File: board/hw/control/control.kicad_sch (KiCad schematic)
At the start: 41 parts, among them J1 stepper #1, J2 stepper #2, J3 buttons, J4 power, J6 AVR-ISP-10, Q1 MMFTP84W, Q2 MMFTP84W, U1 ULN2003A, U2 ULN2003A, U3 ULN2003A, U4 ULN2003A, U5 LM78L05_SO8

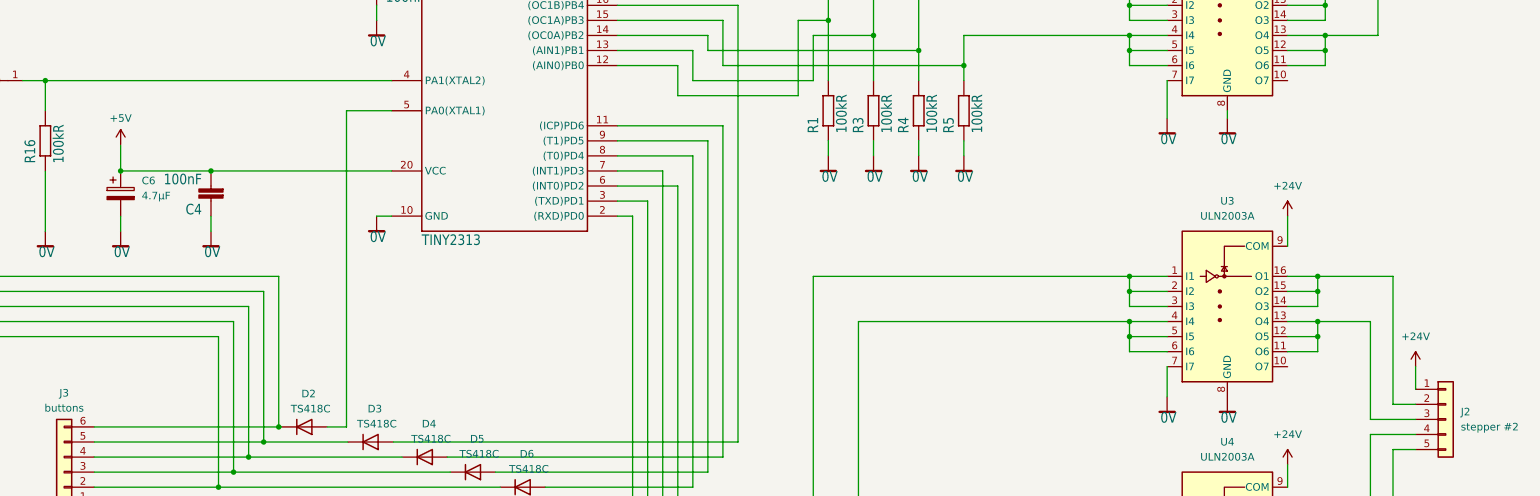
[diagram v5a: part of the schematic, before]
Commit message: added mount holes instead of vias + associated mess
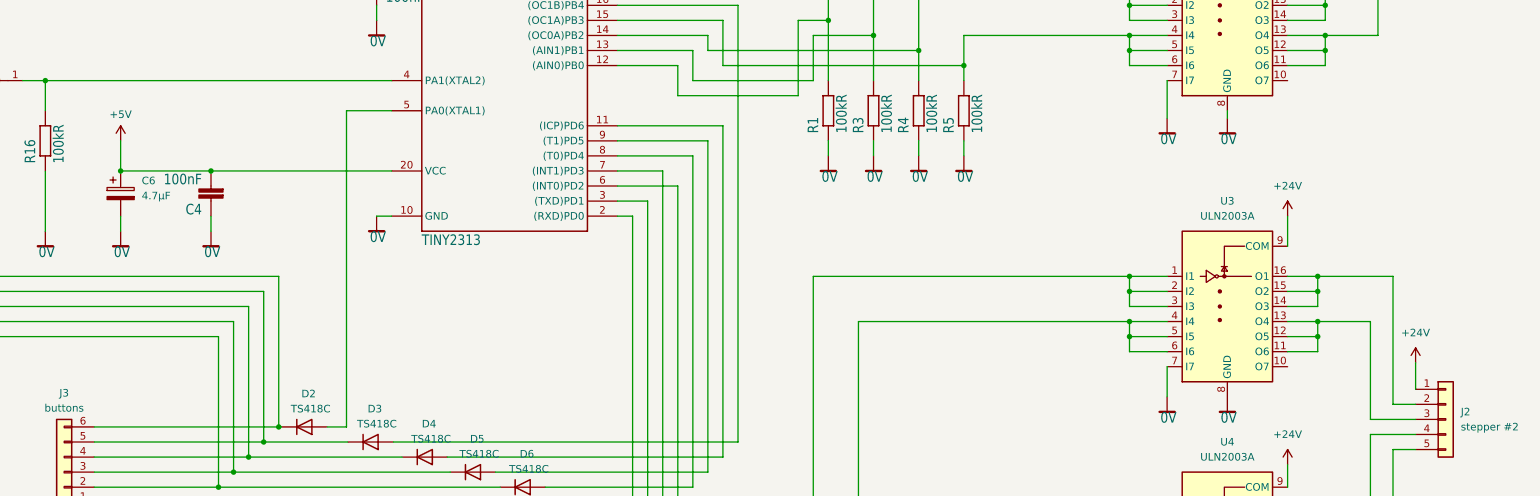
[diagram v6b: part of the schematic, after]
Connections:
- net +5V: now also C4.2, C6.1, U$1.20 (VCC)
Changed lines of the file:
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@@
   (junction (at 213.36 76.2) (diameter 0) (color 0 0 0 0)
   )
+  (junction (at 246.38 34.29) (diameter 0) (color 0 0 0 0)
+  )
+  (junction (at -22.86 64.77) (diameter 0) (color 0 0 0 0)
+  )
+  (junction (at 246.38 76.2) (diameter 0) (color 0 0 0 0)
+  )
+  (junction (at 213.36 29.21) (diameter 0) (color 0 0 0 0)
+  )
+  (junction (at 86.36 60.96) (diameter 0) (color 0 0 0 0)
+  )
+  (junction (at 213.36 68.58) (diameter 0) (color 0 0 0 0)
+  )
+  (junction (at 246.38 68.58) (diameter 0) (color 0 0 0 0)
+  )
+  (junction (at 245.11 160.02) (diameter 0) (color 0 0 0 0)
+  )
+  (junction (at 246.38 36.83) (diameter 0) (color 0 0 0 0)
+  )
   (junction (at 43.18 99.06) (diameter 0) (color 0 0 0 0)
   )
-  (junction (at 246.38 34.29) (diameter 0) (color 0 0 0 0)
-  )
-  (junction (at -22.86 64.77) (diameter 0) (color 0 0 0 0)
-  )
-  (junction (at 246.38 76.2) (diameter 0) (color 0 0 0 0)
-  )
-  (junction (at 213.36 29.21) (diameter 0) (color 0 0 0 0)
-  )
-  (junction (at 86.36 60.96) (diameter 0) (color 0 0 0 0)
-  )
-  (junction (at 213.36 68.58) (diameter 0) (color 0 0 0 0)
-  )
-  (junction (at 246.38 68.58) (diameter 0) (color 0 0 0 0)
-  )
-  (junction (at 245.11 160.02) (diameter 0) (color 0 0 0 0)
-  )
-  (junction (at 246.38 36.83) (diameter 0) (color 0 0 0 0)
-  )
   (junction (at 213.36 26.67) (diameter 0) (color 0 0 0 0)
   )
@@
     (stroke (width 0) (type default))
   )
-  (wire (pts (xy 261.62 132.08) (xy 261.62 135.89))
+  (wire (pts (xy 261.62 131.445) (xy 261.62 135.89))
     (stroke (width 0) (type default))
   )
@@
     (stroke (width 0) (type default))
   )
+  (wire (pts (xy 43.18 93.98) (xy 43.18 99.06))
+    (stroke (width 0) (type default))
+  )
   (wire (pts (xy -40.64 127) (xy 59.69 127))
     (stroke (width 0) (type default))
@@
   )
   (wire (pts (xy 252.095 52.705) (xy 252.095 68.58))
-    (stroke (width 0) (type default))
-  )
-  (wire (pts (xy 43.18 94.742) (xy 43.18 99.06))
     (stroke (width 0) (type default))
   )
@@
     )
   )
-  (symbol (lib_id "power:+24V") (at 261.62 132.08 0) (unit 1)
-    (in_bom yes) (on_board yes) (dnp no)
-    (property "Reference" "#PWR08" (at 261.62 135.89 0)
-      (effects (font (size 1.27 1.27)) hide)
-    )
-    (property "Value" "+24V" (at 261.62 127 0)
+  (symbol (lib_id "power:+24V") (at 261.62 131.445 0) (unit 1)
+    (in_bom yes) (on_board yes) (dnp no)
+    (property "Reference" "#PWR08" (at 261.62 135.255 0)
+      (effects (font (size 1.27 1.27)) hide)
+    )
+    (property "Value" "+24V" (at 261.62 126.365 0)
       (effects (font (size 1.27 1.27)))
     )
-    (property "Footprint" "" (at 261.62 132.08 0)
-      (effects (font (size 1.27 1.27)) hide)
-    )
-    (property "Datasheet" "" (at 261.62 132.08 0)
+    (property "Footprint" "" (at 261.62 131.445 0)
+      (effects (font (size 1.27 1.27)) hide)
+    )
+    (property "Datasheet" "" (at 261.62 131.445 0)
       (effects (font (size 1.27 1.27)) hide)
     )
@@
     )
   )
-  (symbol (lib_id "power:+5V") (at 43.18 94.615 0) (unit 1)
+  (symbol (lib_id "power:+5V") (at 43.18 93.98 0) (unit 1)
     (in_bom yes) (on_board yes) (dnp no) (fields_autoplaced)
-    (property "Reference" "#PWR01" (at 43.18 98.425 0)
-      (effects (font (size 1.27 1.27)) hide)
-    )
-    (property "Value" "+5V" (at 43.18 90.17 0)
+    (property "Reference" "#PWR01" (at 43.18 97.79 0)
+      (effects (font (size 1.27 1.27)) hide)
+    )
+    (property "Value" "+5V" (at 43.18 89.535 0)
       (effects (font (size 1.27 1.27)))
     )
-    (property "Footprint" "" (at 43.18 94.615 0)
-      (effects (font (size 1.27 1.27)) hide)
-    )
-    (property "Datasheet" "" (at 43.18 94.615 0)
-      (effects (font (size 1.27 1.27)) hide)
-    )
+    (property "Footprint" "" (at 43.18 93.98 0)
+      (effects (font (size 1.27 1.27)) hide)
+    )
+    (property "Datasheet" "" (at 43.18 93.98 0)
+      (effects (font (size 1.27 1.27)) hide)
+    )

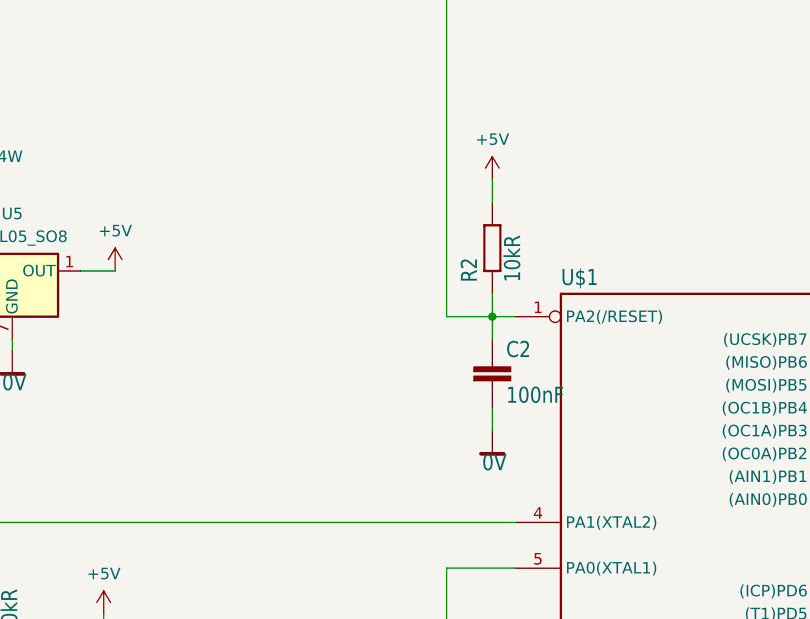
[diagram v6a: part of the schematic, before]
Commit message: added power-on LED to +5V line
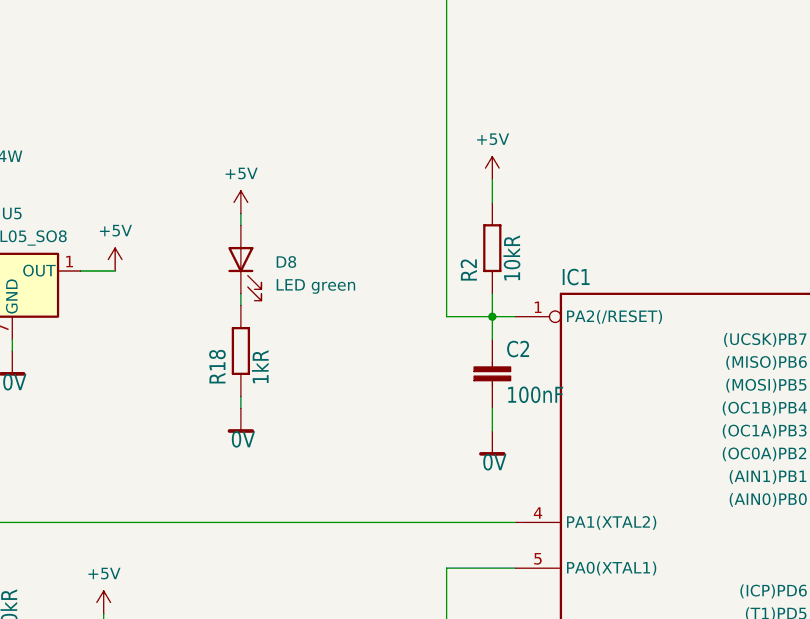
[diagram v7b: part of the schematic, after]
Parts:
- added D8: LED green, LED_SMD:LED_0805_2012Metric_Pad1.15x1.40mm_HandSolder, symbol Device:LED
- added R18: 1kR, Resistor_SMD:R_0805_2012Metric_Pad1.20x1.40mm_HandSolder, symbol control-eagle-import:R-EU_MELF0204W
- renumbered U$1 to IC1
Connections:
- net +5V: now also D8.2 (A)
- net 0V: now also R18.1
- new net: D8.1 (K), R18.2
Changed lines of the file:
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@@
+    (stroke (width 0) (type default))
+  )
+  (wire (pts (xy 58.42 58.42) (xy 58.42 59.69))
     (stroke (width 0) (type default))
   )
@@
     (stroke (width 0) (type default))
   )
+  (wire (pts (xy 58.42 49.53) (xy 58.42 50.8))
+    (stroke (width 0) (type default))
+  )
   (wire (pts (xy 10.795 34.29) (xy 20.32 34.29))
     (stroke (width 0) (type default))
@@
     (stroke (width 0) (type default))
   )
+  (wire (pts (xy 58.42 69.85) (xy 58.42 71.12))
+    (stroke (width 0) (type default))
+  )
   (symbol (lib_id "control-eagle-import:0V") (at 17.78 67.31 0) (unit 1)
     (in_bom yes) (on_board yes) (dnp no)
@@
         (path "/99b3aba4-a2cc-4425-a477-43f3a410d922"
           (reference "R10") (unit 1)
+        )
+      )
+    )
+  )
+  (symbol (lib_id "Device:LED") (at 58.42 54.61 90) (unit 1)
+    (in_bom yes) (on_board yes) (dnp no) (fields_autoplaced)
+    (property "Reference" "D8" (at 62.23 54.9275 90)
+      (effects (font (size 1.27 1.27)) (justify right))
+    )
+    (property "Value" "LED green" (at 62.23 57.4675 90)
+      (effects (font (size 1.27 1.27)) (justify right))
+    )
+    (property "Footprint" "LED_SMD:LED_0805_2012Metric_Pad1.15x1.40mm_HandSolder" (at 58.42 54.61 0)
+      (effects (font (size 1.27 1.27)) hide)
+    )
+    (property "Datasheet" "~" (at 58.42 54.61 0)
+      (effects (font (size 1.27 1.27)) hide)
+    )
+    (pin "1")
+    (pin "2")
+    (instances
+      (project "control"
+        (path "/99b3aba4-a2cc-4425-a477-43f3a410d922"
+          (reference "D8") (unit 1)
         )
       )
@@
     )
   )
+  (symbol (lib_id "control-eagle-import:0V") (at 58.42 73.66 0) (unit 1)
+    (in_bom yes) (on_board yes) (dnp no)
+    (property "Reference" "#SUPPLY021" (at 58.42 73.66 0)
+      (effects (font (size 1.27 1.27)) hide)
+    )
+    (property "Value" "0V" (at 57.277 75.692 0)
+      (effects (font (size 1.778 1.5113)) (justify left bottom))
+    )
+    (property "Footprint" "control:" (at 58.42 73.66 0)
+      (effects (font (size 1.27 1.27)) hide)
+    )
+    (property "Datasheet" "" (at 58.42 73.66 0)
+      (effects (font (size 1.27 1.27)) hide)
+    )
+    (pin "1")
+    (instances
+      (project "control"
+        (path "/99b3aba4-a2cc-4425-a477-43f3a410d922"
+          (reference "#SUPPLY021") (unit 1)
+        )
+      )
+    )
+  )
   (symbol (lib_id "control-eagle-import:R-EU_MELF0204W") (at 177.8 88.9 90) (unit 1)
     (in_bom yes) (on_board yes) (dnp no)
@@
     )
   )
+  (symbol (lib_id "control-eagle-import:R-EU_MELF0204W") (at 58.42 64.77 90) (unit 1)
+    (in_bom yes) (on_board yes) (dnp no)
+    (property "Reference" "R18" (at 56.9214 68.58 0)
+      (effects (font (size 1.778 1.5113)) (justify left bottom))
+    )
+    (property "Value" "1kR" (at 61.722 68.58 0)
+      (effects (font (size 1.778 1.5113)) (justify left bottom))
+    )
+    (property "Footprint" "Resistor_SMD:R_0805_2012Metric_Pad1.20x1.40mm_HandSolder" (at 58.42 64.77 0)
+      (effects (font (size 1.27 1.27)) hide)
+    )
+    (property "Datasheet" "" (at 58.42 64.77 0)
+      (effects (font (size 1.27 1.27)) hide)
+    )
+    (pin "1")
+    (pin "2")
+    (instances
+      (project "control"
+        (path "/99b3aba4-a2cc-4425-a477-43f3a410d922"
+          (reference "R18") (unit 1)
+        )
+      )
+    )
+  )
   (symbol (lib_id "control-eagle-import:0V") (at 229.87 49.53 0) (unit 1)
     (in_bom yes) (on_board yes) (dnp no)
@@
   (symbol (lib_id "control-eagle-import:TINY2313-P") (at 109.22 78.74 0) (unit 1)
     (in_bom yes) (on_board yes) (dnp no)
-    (property "Reference" "U$1" (at 93.98 57.658 0)
+    (property "Reference" "IC1" (at 93.98 57.658 0)
       (effects (font (size 1.778 1.5113)) (justify left bottom))
     )
@@
       (project "control"
         (path "/99b3aba4-a2cc-4425-a477-43f3a410d922"
-          (reference "U$1") (unit 1)
+          (reference "IC1") (unit 1)
         )
       )
@@
         )
       )
+    )
+  )
+  (symbol (lib_id "power:+5V") (at 58.42 49.53 0) (unit 1)
+    (in_bom yes) (on_board yes) (dnp no) (fields_autoplaced)
+    (property "Reference" "#PWR010" (at 58.42 53.34 0)
+      (effects (font (size 1.27 1.27)) hide)
+    )
+    (property "Value" "+5V" (at 58.42 45.085 0)
+      (effects (font (size 1.27 1.27)))
+    )
+    (property "Footprint" "" (at 58.42 49.53 0)
+      (effects (font (size 1.27 1.27)) hide)
+    )
+    (property "Datasheet" "" (at 58.42 49.53 0)
+      (effects (font (size 1.27 1.27)) hide)
+    )
+    (pin "1")
+    (instances
+      (project "control"
+        (path "/99b3aba4-a2cc-4425-a477-43f3a410d922"
+          (reference "#PWR010") (unit 1)
+        )
+      )

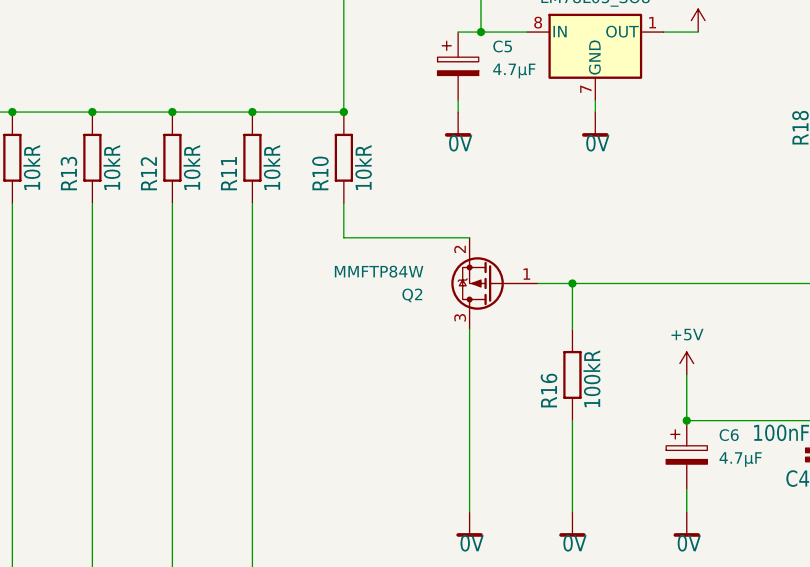
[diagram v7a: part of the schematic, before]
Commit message: replaced P-MOSFET with N-MOSFET to maintain power-on state
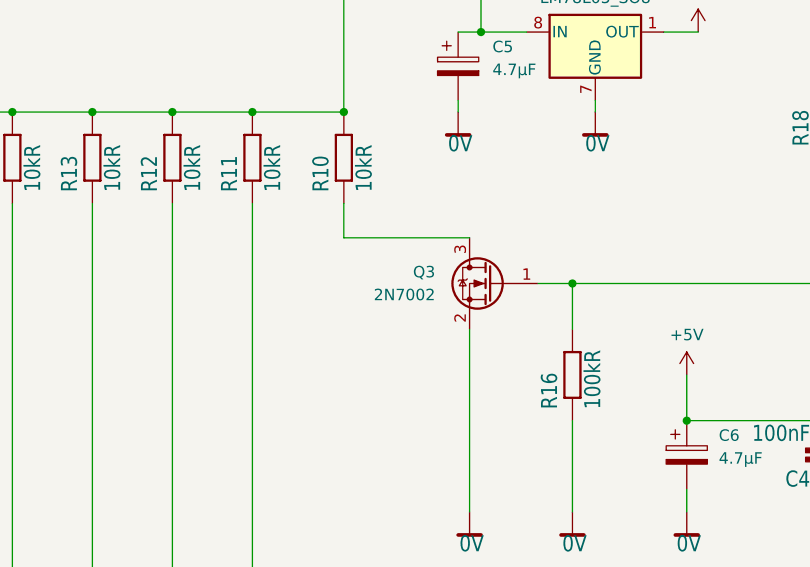
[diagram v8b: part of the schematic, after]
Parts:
- removed Q2: MMFTP84W, Package_TO_SOT_SMD:SOT-323_SC-70, symbol Device:Q_PMOS_GSD
- added Q3: 2N7002, Package_TO_SOT_SMD:SOT-23, symbol Transistor_FET:2N7002
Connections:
- net 0V: now also Q3.2 (S)
- net at R10.1: now also Q3.3 (D)
- net at IC1.4 (PA1(XTAL2)), R16.2: now also Q3.1 (G)
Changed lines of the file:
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@@
+    )
+  )
+  (symbol (lib_id "Transistor_FET:2N7002") (at 21.59 83.82 0) (mirror y) (unit 1)
+    (in_bom yes) (on_board yes) (dnp no) (fields_autoplaced)
+    (property "Reference" "Q3" (at 15.24 82.55 0)
+      (effects (font (size 1.27 1.27)) (justify left))
+    )
+    (property "Value" "2N7002" (at 15.24 85.09 0)
+      (effects (font (size 1.27 1.27)) (justify left))
+    )
+    (property "Footprint" "Package_TO_SOT_SMD:SOT-23" (at 16.51 85.725 0)
+      (effects (font (size 1.27 1.27) italic) (justify left) hide)
+    )
+    (property "Datasheet" "https://www.onsemi.com/pub/Collateral/NDS7002A-D.PDF" (at 21.59 83.82 0)
+      (effects (font (size 1.27 1.27)) (justify left) hide)
+    )
+    (pin "1")
+    (pin "2")
+    (pin "3")
+    (instances
+      (project "control"
+        (path "/99b3aba4-a2cc-4425-a477-43f3a410d922"
+          (reference "Q3") (unit 1)
+        )
+      )
     )
   )
@@
         )
       )
-    )
-  )
-  (symbol (lib_id "Device:Q_PMOS_GSD") (at 21.59 83.82 180) (unit 1)
-    (in_bom yes) (on_board yes) (dnp no)
-    (property "Reference" "Q2" (at 13.97 85.09 0)
-      (effects (font (size 1.27 1.27)) (justify left))
-    )
-    (property "Value" "MMFTP84W" (at 13.97 82.55 0)
-      (effects (font (size 1.27 1.27)) (justify left))
-    )
-    (property "Footprint" "Package_TO_SOT_SMD:SOT-323_SC-70" (at 16.51 86.36 0)
-      (effects (font (size 1.27 1.27)) hide)
-    )
-    (property "Datasheet" "~" (at 21.59 83.82 0)
-      (effects (font (size 1.27 1.27)) hide)
-    )
-    (pin "1")
-    (pin "2")
-    (pin "3")
-    (instances
-      (project "control"
-        (path "/99b3aba4-a2cc-4425-a477-43f3a410d922"
-          (reference "Q2") (unit 1)
-        )
-      )
